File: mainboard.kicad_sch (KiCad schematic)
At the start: 47 parts, among them J1 DRV8833-1, J13 Conn_PCA9685, J14 Conn_01x02, J15 Conn_01x02, J16 Conn_01x02, J18 Screw_Terminal_01x06, J19 Screw_Terminal_01x06, J2 DRV8833-0, J20 Screw_Terminal_01x06, J21 Screw_Terminal_01x06, J22 Screw_Terminal_01x06, J23 Screw_Terminal_01x06, J24 Screw_Terminal_01x04, J25 Screw_Terminal_01x02, J27 Rotary Encoder Conn, J28 Conn_01x02, J3 Conn_01x02, J4 Screw_Terminal_01x06, J5 Screw_Terminal_01x06, J6 VIM4_HEADER, J7 Screw_Terminal_01x06, J8 Screw_Terminal_01x06, Q3 2N7000, Q4 2N7000, U1 MCP23017_SP

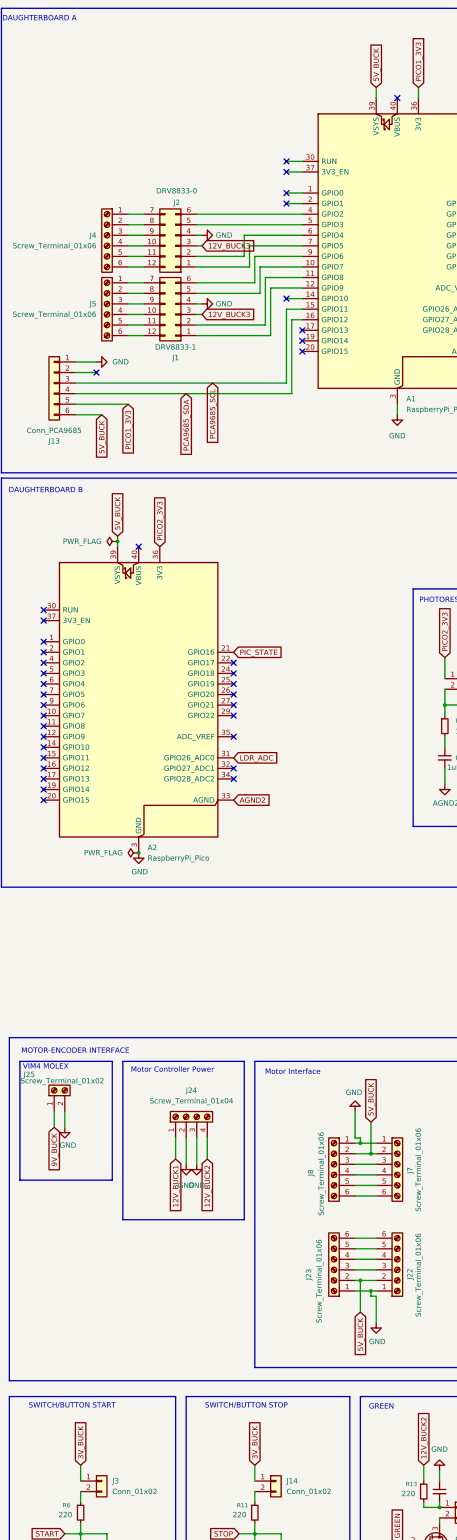
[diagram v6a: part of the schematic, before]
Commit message: Buckboard Beta 1
Ready for Ochoa review
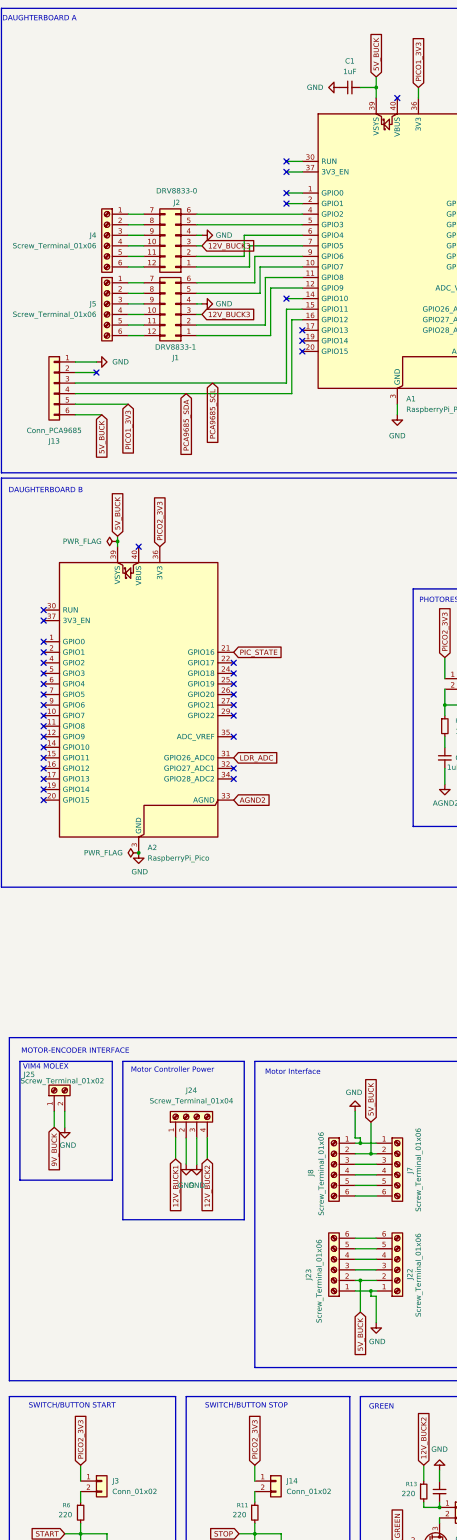
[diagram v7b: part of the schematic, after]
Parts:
- added C1: 1uF, Capacitor_SMD:C_0805_2012Metric, symbol Device:C_Small
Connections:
- net 3V_BUCK is gone; now on net PICO2_3V3: J14.1 (Pin_1), J3.1 (Pin_1)
- net 5V_BUCK: now also C1.2
- net GND: now also C1.1
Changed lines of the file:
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@@
 	)
 	(junction
+		(at 102.87 33.02)
+		(diameter 0)
+		(color 0 0 0 0)
+	)
+	(junction
 		(at 222.25 80.01)
 		(diameter 0)
@@
 	(wire
 		(pts
+			(xy 102.87 33.02) (xy 102.87 35.56)
+		)
+		(stroke
+			(width 0)
+			(type default)
+		)
+	)
+	(wire
+		(pts
 			(xy 181.61 80.01) (xy 180.34 80.01)
 		)
@@
 	(wire
 		(pts
+			(xy 99.06 33.02) (xy 102.87 33.02)
+		)
+		(stroke
+			(width 0)
+			(type default)
+		)
+	)
+	(wire
+		(pts
 			(xy 80.01 389.89) (xy 80.01 388.62)
 		)
@@
 	(wire
 		(pts
-			(xy 102.87 33.02) (xy 102.87 35.56)
+			(xy 102.87 30.48) (xy 102.87 33.02)
 		)
 		(stroke
@@
 		)
 	)
-	(global_label "3V_BUCK"
+	(global_label "PICO2_3V3"
 		(shape input)
-		(at 73.66 364.49 90)
+		(at 31.75 364.49 90)
 		(fields_autoplaced yes)
 		(effects
@@
 		)
 		(property "Intersheetrefs" "${INTERSHEET_REFS}"
-			(at 73.66 353.0986 90)
+			(at 31.75 351.3448 90)
 			(effects
 				(font
@@
 	(global_label "5V_BUCK"
 		(shape input)
-		(at 102.87 33.02 90)
+		(at 102.87 30.48 90)
 		(fields_autoplaced yes)
 		(effects
@@
 		)
 		(property "Intersheetrefs" "${INTERSHEET_REFS}"
-			(at 102.87 21.6286 90)
+			(at 102.87 19.0886 90)
 			(effects
 				(font
@@
 		)
 	)
+	(global_label "PICO2_3V3"
+		(shape input)
+		(at 73.66 364.49 90)
+		(fields_autoplaced yes)
+		(effects
+			(font
+				(size 1.27 1.27)
+			)
+			(justify left)
+		)
+		(property "Intersheetrefs" "${INTERSHEET_REFS}"
+			(at 73.66 351.3448 90)
+			(effects
+				(font
+					(size 1.27 1.27)
+				)
+				(justify left)
+				(hide yes)
+			)
+		)
+	)
 	(global_label "AGND1"
 		(shape input)
@@
 		)
 	)
-	(global_label "3V_BUCK"
-		(shape input)
-		(at 31.75 364.49 90)
-		(fields_autoplaced yes)
-		(effects
-			(font
-				(size 1.27 1.27)
-			)
-			(justify left)
-		)
-		(property "Intersheetrefs" "${INTERSHEET_REFS}"
-			(at 31.75 353.0986 90)
-			(effects
-				(font
-					(size 1.27 1.27)
-				)
-				(justify left)
-				(hide yes)
-			)
-		)
-	)
 	(global_label "PCA9685_SDA"
 		(shape input)
@@
 	)
 	(symbol
+		(lib_id "Device:C_Small")
+		(at 96.52 33.02 90)
+		(unit 1)
+		(exclude_from_sim no)
+		(in_bom yes)
+		(on_board yes)
+		(dnp no)
+		(fields_autoplaced yes)
+		(property "Reference" "C1"
+			(at 96.5263 26.67 90)
+			(effects
+				(font
+					(size 1.27 1.27)
+				)
+			)
+		)
+		(property "Value" "1uF"
+			(at 96.5263 29.21 90)
+			(effects
+				(font
+					(size 1.27 1.27)
+				)
+			)
+		)
+		(property "Footprint" "Capacitor_SMD:C_0805_2012Metric"
+			(at 96.52 33.02 0)
+			(effects
+				(font
+					(size 1.27 1.27)
+				)
+				(hide yes)
+			)
+		)
+		(property "Datasheet" "~"
+			(at 96.52 33.02 0)
+			(effects
+				(font
+					(size 1.27 1.27)
+				)
+				(hide yes)
+			)
+		)
+		(property "Description" "Unpolarized capacitor, small symbol"
+			(at 96.52 33.02 0)
+			(effects
+				(font
+					(size 1.27 1.27)
+				)
+				(hide yes)
+			)
+		)
+		(pin "2"
+		)
+		(pin "1"
+		)
+		(instances
+			(project ""
+				(path "/c17272df-bb38-44d5-9de0-abe2e6f0941d"
+					(reference "C1")
+					(unit 1)
+				)
+			)
+		)
+	)
+	(symbol
 		(lib_id "power:GND")
 		(at 119.38 200.66 0)
@@
 					(unit 1)
 				)
+			)
+		)
+	)
+	(symbol
+		(lib_id "power:GND")
+		(at 93.98 33.02 270)
+		(unit 1)
+		(exclude_from_sim no)
+		(in_bom yes)
+		(on_board yes)
+		(dnp no)
+		(fields_autoplaced yes)
+		(property "Reference" "#PWR021"
+			(at 87.63 33.02 0)
+			(effects
+				(font
+					(size 1.27 1.27)
+				)
+				(hide yes)
+			)
+		)
+		(property "Value" "GND"
+			(at 90.17 33.0199 90)
+			(effects
+				(font
+					(size 1.27 1.27)
+				)
+				(justify right)
+			)
+		)
+		(property "Footprint" ""
+			(at 93.98 33.02 0)
+			(effects
+				(font
+					(size 1.27 1.27)
+				)
+				(hide yes)
+			)
+		)
+		(property "Datasheet" ""
+			(at 93.98 33.02 0)
+			(effects
+				(font
+					(size 1.27 1.27)
+				)
+				(hide yes)
+			)
+		)
+		(property "Description" "Power symbol creates a global label with name \"GND\" , ground"
+			(at 93.98 33.02 0)
+			(effects
+				(font
+					(size 1.27 1.27)
+				)
+				(hide yes)
+			)
+		)
+		(pin "1"
+		)
+		(instances
+			(project ""
+				(path "/c17272df-bb38-44d5-9de0-abe2e6f0941d"
+					(reference "#PWR021")
+					(unit 1)
+				)

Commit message: V1.2
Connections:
- net 5V_BUCK: no longer J13.6 (Pin_6)
- net COLL(en/dis): now also J6.22 (Pin_22); no longer J6.38 (Pin_38)
- net PIC_STATE: now also J6.36 (Pin_36); no longer J6.31 (Pin_31)
- net SORT(en/dis): now also J6.30 (Pin_30); no longer J6.39 (Pin_39)
- net TOTEM-EXTEND: now also J6.31 (Pin_31); no longer J6.32 (Pin_32)
- net BOOM(ext/ret): no longer names the net of J6.33 (Pin_33)
- no-connect marks 69 -> 70
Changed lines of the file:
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@@
 	)
 	(no_connect
+		(at 33.02 111.76)
+	)
+	(no_connect
 		(at 22.86 199.39)
 	)
@@
 	)
 	(no_connect
-		(at 308.61 179.07)
-	)
-	(no_connect
-		(at 308.61 143.51)
+		(at 308.61 186.69)
 	)
 	(no_connect
@@
 	)
 	(no_connect
-		(at 68.58 181.61)
+		(at 308.61 184.15)
 	)
 	(no_connect
-		(at 68.58 179.07)
+		(at 68.58 181.61)
 	)
 	(no_connect
-		(at 308.61 163.83)
+		(at 68.58 179.07)
 	)
 	(no_connect
@@
 	)
 	(no_connect
+		(at 308.61 168.91)
+	)
+	(no_connect
 		(at 288.29 143.51)
 	)
@@
 	)
 	(no_connect
+		(at 308.61 171.45)
+	)
+	(no_connect
 		(at 22.86 171.45)
 	)
@@
 	)
 	(no_connect
-		(at 308.61 181.61)
-	)
-	(no_connect
 		(at 22.86 191.77)
 	)
@@
 	(wire
 		(pts
+			(xy 30.48 111.76) (xy 33.02 111.76)
+		)
+		(stroke
+			(width 0)
+			(type default)
+		)
+	)
+	(wire
+		(pts
+			(xy 306.07 168.91) (xy 308.61 168.91)
+		)
+		(stroke
+			(width 0)
+			(type default)
+		)
+	)
+	(wire
+		(pts
 			(xy 140.97 289.56) (xy 142.24 289.56)
 		)
@@
 	(wire
 		(pts
-			(xy 306.07 186.69) (xy 308.61 186.69)
-		)
-		(stroke
-			(width 0)
-			(type default)
-		)
-	)
-	(wire
-		(pts
 			(xy 59.69 66.04) (xy 85.09 66.04)
 		)
@@
 	(wire
 		(pts
-			(xy 306.07 179.07) (xy 308.61 179.07)
-		)
-		(stroke
-			(width 0)
-			(type default)
-		)
-	)
-	(wire
-		(pts
 			(xy 167.64 80.01) (xy 167.64 68.58)
 		)
@@
 	(wire
 		(pts
+			(xy 306.07 186.69) (xy 308.61 186.69)
+		)
+		(stroke
+			(width 0)
+			(type default)
+		)
+	)
+	(wire
+		(pts
 			(xy 224.79 77.47) (xy 243.84 77.47)
 		)
@@
 	(wire
 		(pts
-			(xy 306.07 184.15) (xy 308.61 184.15)
-		)
-		(stroke
-			(width 0)
-			(type default)
-		)
-	)
-	(wire
-		(pts
 			(xy 72.39 71.12) (xy 72.39 76.2)
 		)
@@
 	(wire
 		(pts
-			(xy 306.07 181.61) (xy 308.61 181.61)
-		)
-		(stroke
-			(width 0)
-			(type default)
-		)
-	)
-	(wire
-		(pts
 			(xy 118.11 377.19) (xy 118.11 378.46)
 		)
@@
 	(wire
 		(pts
-			(xy 308.61 166.37) (xy 306.07 166.37)
-		)
-		(stroke
-			(width 0)
-			(type default)
-		)
-	)
-	(wire
-		(pts
 			(xy 97.79 285.75) (xy 99.06 285.75)
 		)
@@
 	(wire
 		(pts
-			(xy 308.61 168.91) (xy 306.07 168.91)
-		)
-		(stroke
-			(width 0)
-			(type default)
-		)
-	)
-	(wire
-		(pts
 			(xy 306.07 189.23) (xy 309.88 189.23)
 		)
@@
 	(wire
 		(pts
-			(xy 30.48 111.76) (xy 36.83 111.76)
-		)
-		(stroke
-			(width 0)
-			(type default)
-		)
-	)
-	(wire
-		(pts
 			(xy 43.18 68.58) (xy 46.99 68.58)
 		)
@@
 	(wire
 		(pts
+			(xy 306.07 184.15) (xy 308.61 184.15)
+		)
+		(stroke
+			(width 0)
+			(type default)
+		)
+	)
+	(wire
+		(pts
 			(xy 138.43 327.66) (xy 138.43 320.04)
 		)
@@
 	(wire
 		(pts
+			(xy 306.07 179.07) (xy 308.61 179.07)
+		)
+		(stroke
+			(width 0)
+			(type default)
+		)
+	)
+	(wire
+		(pts
 			(xy 288.29 148.59) (xy 293.37 148.59)
 		)
@@
 	(wire
 		(pts
+			(xy 306.07 166.37) (xy 308.61 166.37)
+		)
+		(stroke
+			(width 0)
+			(type default)
+		)
+	)
+	(wire
+		(pts
 			(xy 152.4 384.81) (xy 152.4 386.08)
 		)
@@
 	(global_label "COLL(en{slash}dis)"
 		(shape input)
-		(at 308.61 184.15 0)
+		(at 308.61 143.51 0)
 		(fields_autoplaced yes)
 		(effects
@@
 		)
 		(property "Intersheetrefs" "${INTERSHEET_REFS}"
-			(at 324.2953 184.15 0)
+			(at 324.2953 143.51 0)
 			(effects
 				(font
@@
 	(global_label "SORT(en{slash}dis)"
 		(shape input)
-		(at 308.61 186.69 0)
+		(at 308.61 163.83 0)
 		(fields_autoplaced yes)
 		(effects
@@
 		)
 		(property "Intersheetrefs" "${INTERSHEET_REFS}"
-			(at 324.4162 186.69 0)
+			(at 324.4162 163.83 0)
 			(effects
 				(font
@@
 	(global_label "TOTEM-EXTEND"
 		(shape input)
-		(at 308.61 168.91 0)
+		(at 308.61 166.37 0)
 		(fields_autoplaced yes)
 		(effects
@@
 		)
 		(property "Intersheetrefs" "${INTERSHEET_REFS}"
-			(at 326.1093 168.91 0)
+			(at 326.1093 166.37 0)
 			(effects
 				(font
@@
 		)
 	)
-	(global_label "BOOM(ext{slash}ret)"
-		(shape input)
-		(at 308.61 171.45 0)
-		(fields_autoplaced yes)
-		(effects
-			(font
-				(size 1.27 1.27)
-			)
-			(justify left)
-		)
-		(property "Intersheetrefs" "${INTERSHEET_REFS}"
-			(at 325.4444 171.45 0)
-			(effects
-				(font
-					(size 1.27 1.27)
-				)
-				(justify left)
-				(hide yes)
-			)
-		)
-	)
 	(global_label "CP-R-ENDSTOP0"
 		(shape input)
@@
 		)
 	)
-	(global_label "5V_BUCK"
-		(shape input)
-		(at 36.83 111.76 270)
-		(fields_autoplaced yes)
-		(effects
-			(font
-				(size 1.27 1.27)
-			)
-			(justify right)
-		)
-		(property "Intersheetrefs" "${INTERSHEET_REFS}"
-			(at 36.83 123.1514 90)
-			(effects
-				(font
-					(size 1.27 1.27)
-				)
-				(justify right)
-				(hide yes)
-			)
-		)
-	)
 	(global_label "PICO1_3V3"
 		(shape input)
@@
 	(global_label "PIC_STATE"
 		(shape input)
-		(at 308.61 166.37 0)
+		(at 308.61 179.07 0)
 		(fields_autoplaced yes)
 		(effects
@@
 		)
 		(property "Intersheetrefs" "${INTERSHEET_REFS}"
-			(at 321.0899 166.37 0)
+			(at 321.0899 179.07 0)
 			(effects
 				(font
